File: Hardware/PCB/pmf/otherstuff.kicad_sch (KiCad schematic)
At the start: 66 parts, among them J10 Synth_power_2x5, J11 Conn_02x07_Odd_Even, J12 AudioJack2, J13 Conn_02x07_Odd_Even, J14 Conn_02x07_Odd_Even, J5 AudioJack2, J6 AudioJack2, J7 AudioJack2, J8 AudioJack2, J9 AudioJack2, SW1 SW_Rotary12, U2 TL072

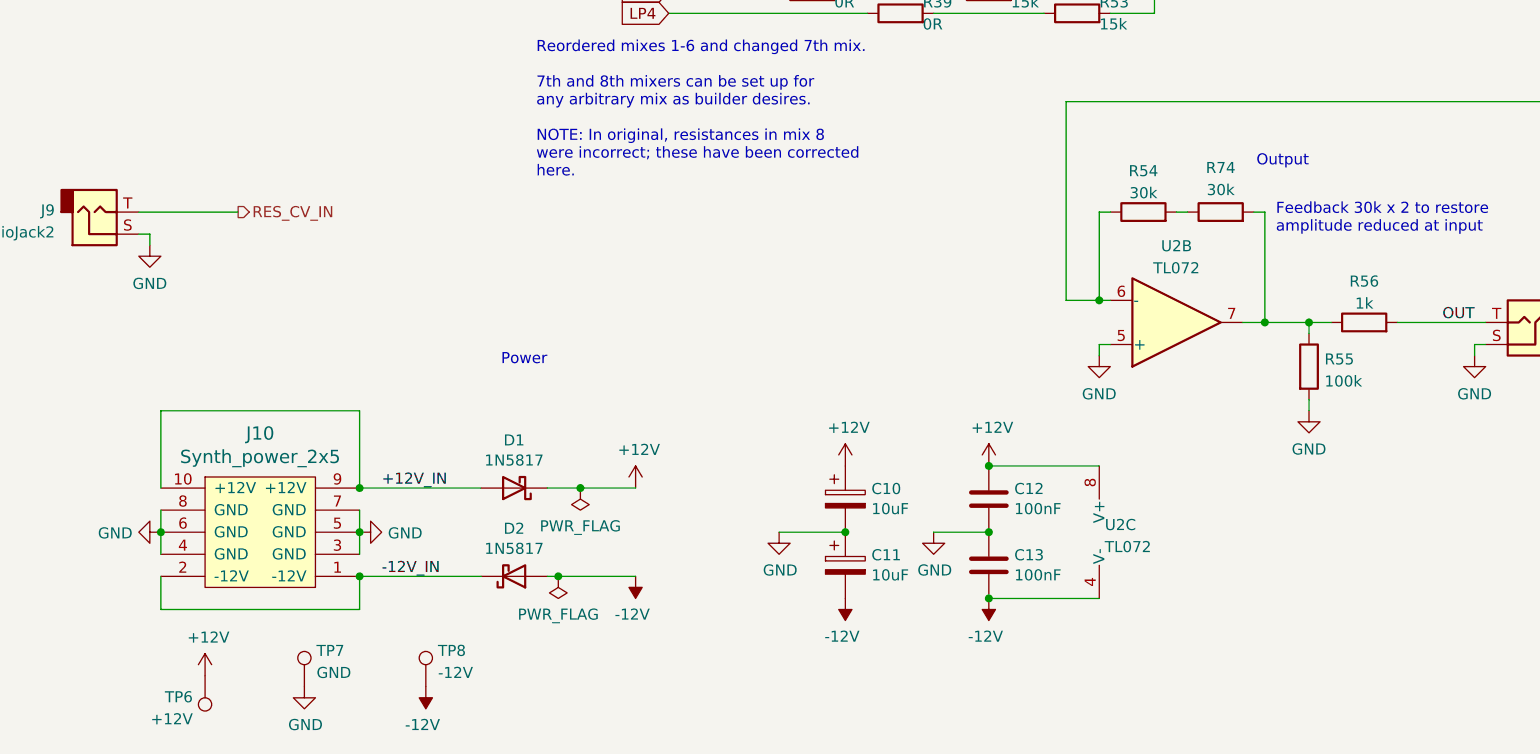
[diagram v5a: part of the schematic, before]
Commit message: CVf test point; disambiguate heirarchical symbols
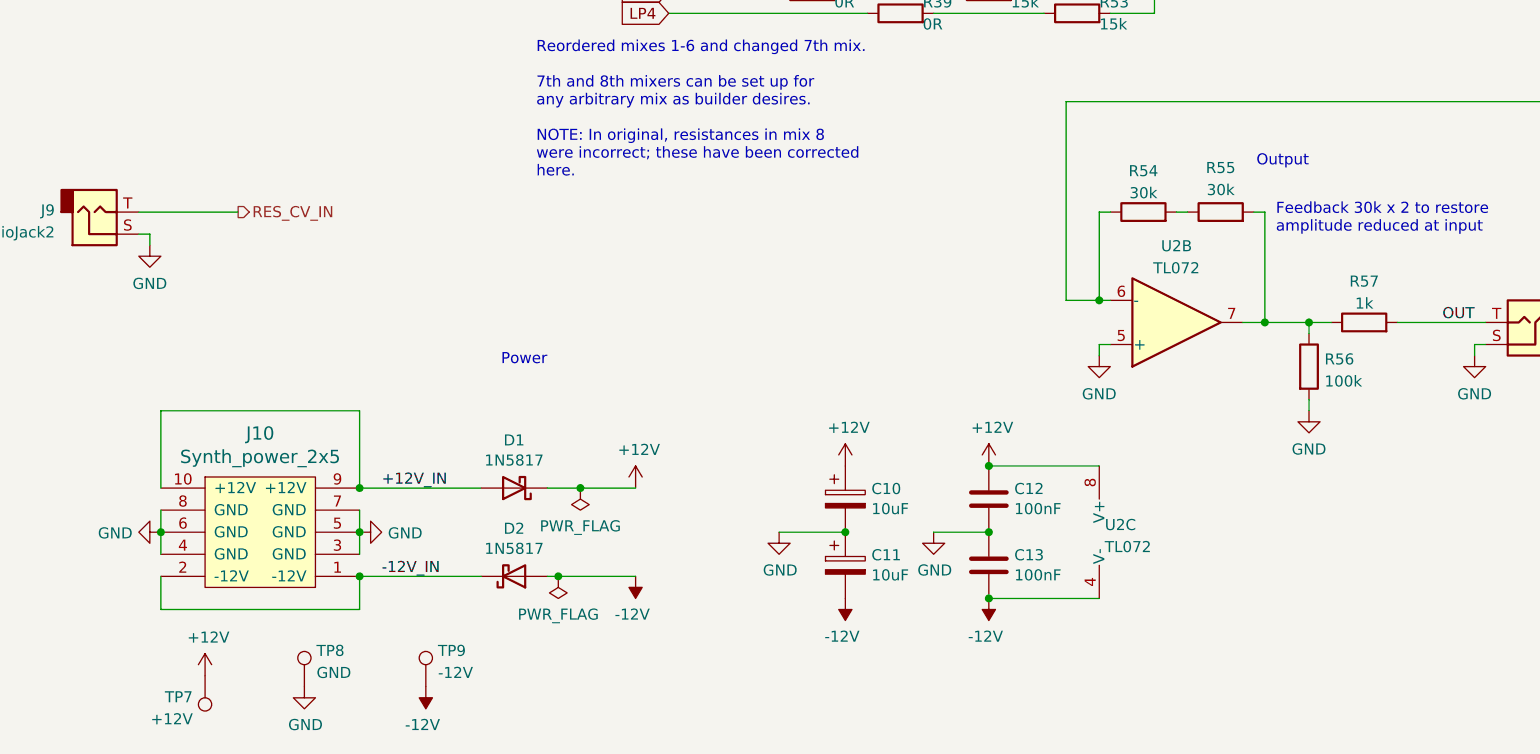
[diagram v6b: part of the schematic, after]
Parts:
- renumbered R74 to R55, R55 to R56, R56 to R57, TP6 to TP7, TP7 to TP8, TP8 to TP9
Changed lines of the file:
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@@
   (symbol (lib_id "AO_symbols:R") (at 172.72 160.02 0) (unit 1)
     (in_bom yes) (on_board yes) (dnp no) (fields_autoplaced)
-    (property "Reference" "R55" (at 174.498 159.1853 0)
+    (property "Reference" "R56" (at 174.498 159.1853 0)
       (effects (font (size 1.27 1.27)) (justify left))
     )
@@
       (project "pmf"
         (path "/1fce46f5-2003-4c7e-915f-b9b7dfc679d7/a180c6ca-d86a-4fef-be09-a6b0b94046eb"
-          (reference "R55") (unit 1)
+          (reference "R56") (unit 1)
         )
       )
@@
   (symbol (lib_id "AO_symbols:R") (at 179.07 154.94 90) (unit 1)
     (in_bom yes) (on_board yes) (dnp no) (fields_autoplaced)
-    (property "Reference" "R56" (at 179.07 150.2242 90)
+    (property "Reference" "R57" (at 179.07 150.2242 90)
       (effects (font (size 1.27 1.27)))
     )
@@
       (project "pmf"
         (path "/1fce46f5-2003-4c7e-915f-b9b7dfc679d7/a180c6ca-d86a-4fef-be09-a6b0b94046eb"
-          (reference "R56") (unit 1)
+          (reference "R57") (unit 1)
         )
       )
@@
   (symbol (lib_id "AO_symbols:TestPoint") (at 57.15 196.85 0) (unit 1)
     (in_bom no) (on_board yes) (dnp no) (fields_autoplaced)
-    (property "Reference" "TP7" (at 58.547 192.7133 0)
+    (property "Reference" "TP8" (at 58.547 192.7133 0)
       (effects (font (size 1.27 1.27)) (justify left))
     )
@@
       (project "pmf"
         (path "/1fce46f5-2003-4c7e-915f-b9b7dfc679d7/a180c6ca-d86a-4fef-be09-a6b0b94046eb"
-          (reference "TP7") (unit 1)
+          (reference "TP8") (unit 1)
         )
       )
@@
   (symbol (lib_id "AO_symbols:TestPoint") (at 71.12 196.85 0) (unit 1)
     (in_bom no) (on_board yes) (dnp no) (fields_autoplaced)
-    (property "Reference" "TP8" (at 72.517 192.7133 0)
+    (property "Reference" "TP9" (at 72.517 192.7133 0)
       (effects (font (size 1.27 1.27)) (justify left))
     )
@@
       (project "pmf"
         (path "/1fce46f5-2003-4c7e-915f-b9b7dfc679d7/a180c6ca-d86a-4fef-be09-a6b0b94046eb"
-          (reference "TP8") (unit 1)
+          (reference "TP9") (unit 1)
         )
       )
@@
   (symbol (lib_id "AO_symbols:R") (at 162.56 142.24 90) (unit 1)
     (in_bom yes) (on_board yes) (dnp no) (fields_autoplaced)
-    (property "Reference" "R74" (at 162.56 137.16 90)
+    (property "Reference" "R55" (at 162.56 137.16 90)
       (effects (font (size 1.27 1.27)))
     )
@@
       (project "pmf"
         (path "/1fce46f5-2003-4c7e-915f-b9b7dfc679d7/a180c6ca-d86a-4fef-be09-a6b0b94046eb"
-          (reference "R74") (unit 1)
+          (reference "R55") (unit 1)
         )
       )
@@
   (symbol (lib_id "AO_symbols:TestPoint") (at 45.72 195.58 0) (mirror x) (unit 1)
     (in_bom no) (on_board yes) (dnp no) (fields_autoplaced)
-    (property "Reference" "TP6" (at 44.323 198.0473 0)
+    (property "Reference" "TP7" (at 44.323 198.0473 0)
       (effects (font (size 1.27 1.27)) (justify right))
     )
@@
       (project "pmf"
         (path "/1fce46f5-2003-4c7e-915f-b9b7dfc679d7/a180c6ca-d86a-4fef-be09-a6b0b94046eb"
-          (reference "TP6") (unit 1)
-        )
-      )
+          (reference "TP7") (unit 1)
+        )
+      )

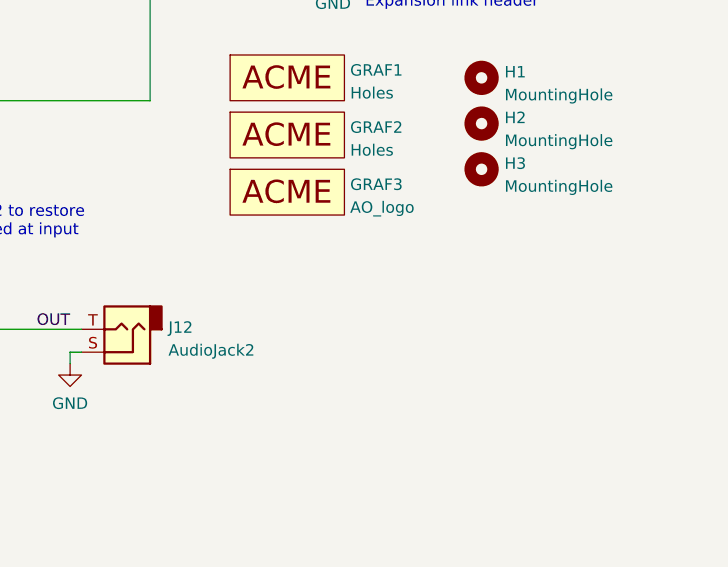
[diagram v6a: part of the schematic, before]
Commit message: Hardware symbols test
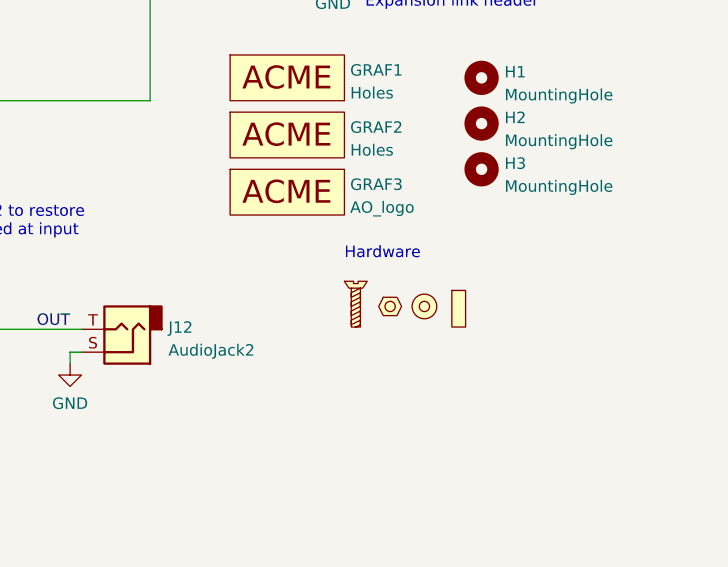
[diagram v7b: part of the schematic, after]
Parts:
- added M1: screw, symbol AO_symbols:Screw
- added M2: nut, symbol AO_symbols:Nut
- added M3: washer, symbol AO_symbols:Washer
- added M4: spacer, symbol AO_symbols:Spacer
- R28, R37, R43, R51: footprint pmf:R_Axial_DNF_L6.3mm_P10.16mm_Horizontal -> AO_tht:R_Axial_DIN0207_L6.3mm_D2.5mm_P10.16mm_Horizontal
- R30, R39, R42, R44, R50, R52: footprint pmf:Wire_Jumper_10.16 -> AO_tht:R_Axial_DIN0207_L6.3mm_D2.5mm_P10.16mm_Horizontal
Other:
- note added: "Hardware"
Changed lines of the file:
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@@
     (effects (font (size 1.27 1.27)) (justify right bottom))
+  )
+  (text "Hardware" (at 222.25 147.32 0)
+    (effects (font (size 1.27 1.27)) (justify left bottom))
   )
   (text "4 pole LP: {0, 0, 0, 0, 1}" (at 114.3 34.29 0)
@@
       (effects (font (size 1.27 1.27)) (justify right))
     )
-    (property "Footprint" "pmf:R_Axial_DNF_L6.3mm_P10.16mm_Horizontal" (at 146.05 104.648 90)
+    (property "Footprint" "AO_tht:R_Axial_DIN0207_L6.3mm_D2.5mm_P10.16mm_Horizontal" (at 146.05 104.648 90)
       (effects (font (size 1.27 1.27)) hide)
     )
@@
       (effects (font (size 1.27 1.27)) (justify right))
     )
-    (property "Footprint" "pmf:Wire_Jumper_10.16" (at 135.89 113.538 90)
+    (property "Footprint" "AO_tht:R_Axial_DIN0207_L6.3mm_D2.5mm_P10.16mm_Horizontal" (at 135.89 113.538 90)
       (effects (font (size 1.27 1.27)) hide)
     )
@@
       (effects (font (size 1.27 1.27)) (justify right))
     )
-    (property "Footprint" "pmf:Wire_Jumper_10.16" (at 135.89 97.028 90)
+    (property "Footprint" "AO_tht:R_Axial_DIN0207_L6.3mm_D2.5mm_P10.16mm_Horizontal" (at 135.89 97.028 90)
       (effects (font (size 1.27 1.27)) hide)
     )
@@
       (effects (font (size 1.27 1.27)) (justify right))
     )
-    (property "Footprint" "pmf:Wire_Jumper_10.16" (at 146.05 116.078 90)
+    (property "Footprint" "AO_tht:R_Axial_DIN0207_L6.3mm_D2.5mm_P10.16mm_Horizontal" (at 146.05 116.078 90)
       (effects (font (size 1.27 1.27)) hide)
     )
@@
     )
   )
+  (symbol (lib_id "AO_symbols:Washer") (at 231.14 152.4 0) (unit 1)
+    (in_bom yes) (on_board no) (dnp no) (fields_autoplaced)
+    (property "Reference" "M3" (at 231.394 148.082 0)
+      (effects (font (size 1.27 1.27)) hide)
+    )
+    (property "Value" "washer" (at 231.394 149.86 0)
+      (effects (font (size 1.27 1.27)) hide)
+    )
+    (property "Footprint" "" (at 231.14 152.4 0)
+      (effects (font (size 1.27 1.27)) hide)
+    )
+    (property "Datasheet" "" (at 231.14 152.4 0)
+      (effects (font (size 1.27 1.27)) hide)
+    )
+    (property "Description" "M3 washer" (at 231.14 152.4 0)
+      (effects (font (size 1.27 1.27)) hide)
+    )
+    (instances
+      (project "pmf"
+        (path "/1fce46f5-2003-4c7e-915f-b9b7dfc679d7/a180c6ca-d86a-4fef-be09-a6b0b94046eb"
+          (reference "M3") (unit 1)
+        )
+      )
+    )
+  )
   (symbol (lib_id "AO_symbols:R") (at 146.05 97.79 90) (unit 1)
     (in_bom yes) (on_board yes) (dnp no)
@@
       (effects (font (size 1.27 1.27)) (justify right))
     )
-    (property "Footprint" "pmf:Wire_Jumper_10.16" (at 146.05 99.568 90)
+    (property "Footprint" "AO_tht:R_Axial_DIN0207_L6.3mm_D2.5mm_P10.16mm_Horizontal" (at 146.05 99.568 90)
       (effects (font (size 1.27 1.27)) hide)
     )
@@
     )
   )
+  (symbol (lib_id "AO_symbols:Spacer") (at 234.95 152.4 0) (unit 1)
+    (in_bom yes) (on_board no) (dnp no) (fields_autoplaced)
+    (property "Reference" "M4" (at 234.95 148.082 0)
+      (effects (font (size 1.27 1.27)) hide)
+    )
+    (property "Value" "spacer" (at 234.95 149.606 0)
+      (effects (font (size 1.27 1.27)) hide)
+    )
+    (property "Footprint" "" (at 234.95 152.4 0)
+      (effects (font (size 1.27 1.27)) hide)
+    )
+    (property "Datasheet" "" (at 234.95 152.4 0)
+      (effects (font (size 1.27 1.27)) hide)
+    )
+    (property "Description" "M3 spacer FF 10 mm" (at 234.95 152.4 0)
+      (effects (font (size 1.27 1.27)) hide)
+    )
+    (instances
+      (project "pmf"
+        (path "/1fce46f5-2003-4c7e-915f-b9b7dfc679d7/a180c6ca-d86a-4fef-be09-a6b0b94046eb"
+          (reference "M4") (unit 1)
+        )
+      )
+    )
+  )
   (symbol (lib_id "AO_symbols:R") (at 115.57 100.33 90) (unit 1)
     (in_bom no) (on_board yes) (dnp yes)
@@
       (effects (font (size 1.27 1.27)) (justify right))
     )
-    (property "Footprint" "pmf:R_Axial_DNF_L6.3mm_P10.16mm_Horizontal" (at 115.57 102.108 90)
+    (property "Footprint" "AO_tht:R_Axial_DIN0207_L6.3mm_D2.5mm_P10.16mm_Horizontal" (at 115.57 102.108 90)
       (effects (font (size 1.27 1.27)) hide)
     )
@@
       (effects (font (size 1.27 1.27)) (justify right))
     )
-    (property "Footprint" "pmf:R_Axial_DNF_L6.3mm_P10.16mm_Horizontal" (at 125.73 104.648 90)
+    (property "Footprint" "AO_tht:R_Axial_DIN0207_L6.3mm_D2.5mm_P10.16mm_Horizontal" (at 125.73 104.648 90)
       (effects (font (size 1.27 1.27)) hide)
     )
@@
       (effects (font (size 1.27 1.27)) (justify right))
     )
-    (property "Footprint" "pmf:R_Axial_DNF_L6.3mm_P10.16mm_Horizontal" (at 135.89 102.108 90)
+    (property "Footprint" "AO_tht:R_Axial_DIN0207_L6.3mm_D2.5mm_P10.16mm_Horizontal" (at 135.89 102.108 90)
       (effects (font (size 1.27 1.27)) hide)
     )
@@
       (effects (font (size 1.27 1.27)) (justify right))
     )
-    (property "Footprint" "pmf:Wire_Jumper_10.16" (at 115.57 118.618 90)
+    (property "Footprint" "AO_tht:R_Axial_DIN0207_L6.3mm_D2.5mm_P10.16mm_Horizontal" (at 115.57 118.618 90)
       (effects (font (size 1.27 1.27)) hide)
     )
@@
         (path "/1fce46f5-2003-4c7e-915f-b9b7dfc679d7/a180c6ca-d86a-4fef-be09-a6b0b94046eb"
           (reference "TP9") (unit 1)
+        )
+      )
+    )
+  )
+  (symbol (lib_id "AO_symbols:Nut") (at 227.33 152.4 0) (unit 1)
+    (in_bom yes) (on_board no) (dnp no) (fields_autoplaced)
+    (property "Reference" "M2" (at 227.33 148.336 0)
+      (effects (font (size 1.27 1.27)) hide)
+    )
+    (property "Value" "nut" (at 227.33 150.114 0)
+      (effects (font (size 1.27 1.27)) hide)
+    )
+    (property "Footprint" "" (at 227.33 152.4 0)
+      (effects (font (size 1.27 1.27)) hide)
+    )
+    (property "Datasheet" "" (at 227.33 152.4 0)
+      (effects (font (size 1.27 1.27)) hide)
+    )
+    (property "Description" "M3 nut" (at 227.33 152.4 0)
+      (effects (font (size 1.27 1.27)) hide)
+    )
+    (instances
+      (project "pmf"
+        (path "/1fce46f5-2003-4c7e-915f-b9b7dfc679d7/a180c6ca-d86a-4fef-be09-a6b0b94046eb"
+          (reference "M2") (unit 1)
         )
       )
@@
     )
   )
+  (symbol (lib_id "AO_symbols:Screw") (at 223.52 152.4 0) (unit 1)
+    (in_bom yes) (on_board no) (dnp no) (fields_autoplaced)
+    (property "Reference" "M1" (at 223.52 147.32 0)
+      (effects (font (size 1.27 1.27)) hide)
+    )
+    (property "Value" "screw" (at 223.774 148.59 0)
+      (effects (font (size 1.27 1.27)) hide)
+    )
+    (property "Footprint" "" (at 223.52 152.4 0)
+      (effects (font (size 1.27 1.27)) hide)
+    )
+    (property "Datasheet" "" (at 223.52 152.4 0)
+      (effects (font (size 1.27 1.27)) hide)
+    )
+    (property "Description" "M3 machine screw 6 mm" (at 223.52 152.4 0)
+      (effects (font (size 1.27 1.27)) hide)
+    )
+    (instances
+      (project "pmf"
+        (path "/1fce46f5-2003-4c7e-915f-b9b7dfc679d7/a180c6ca-d86a-4fef-be09-a6b0b94046eb"
+          (reference "M1") (unit 1)
+        )
+      )
+    )
+  )
   (symbol (lib_id "AO_symbols:MountingHole") (at 237.49 137.16 0) (unit 1)
     (in_bom no) (on_board yes) (dnp no) (fields_autoplaced)
@@
       (effects (font (size 1.27 1.27)) (justify right))
     )
-    (property "Footprint" "pmf:Wire_Jumper_10.16" (at 125.73 121.158 90)
-      (effects (font (size 1.27 1.27)) hide)
-    )
+    (property "Footprint" "AO_tht:R_Axial_DIN0207_L6.3mm_D2.5mm_P10.16mm_Horizontal" (at 125.73 121.158 90)
+      (effects (font (size 1.27 1.27)) hide)
+    )

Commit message: Return to smaller trimmer values; make core schematic clearer; restore munged footprints
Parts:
- R28, R37, R43, R51: footprint AO_tht:R_Axial_DIN0207_L6.3mm_D2.5mm_P10.16mm_Horizontal -> pmf:R_Axial_DNF_L6.3mm_P10.16mm_Horizontal
- R30, R39, R42, R44, R50, R52: footprint AO_tht:R_Axial_DIN0207_L6.3mm_D2.5mm_P10.16mm_Horizontal -> pmf:Wire_Jumper_10.16
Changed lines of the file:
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@@
       (effects (font (size 1.27 1.27)) (justify right))
     )
-    (property "Footprint" "AO_tht:R_Axial_DIN0207_L6.3mm_D2.5mm_P10.16mm_Horizontal" (at 146.05 104.648 90)
+    (property "Footprint" "pmf:R_Axial_DNF_L6.3mm_P10.16mm_Horizontal" (at 146.05 104.648 90)
       (effects (font (size 1.27 1.27)) hide)
     )
@@
       (effects (font (size 1.27 1.27)) (justify right))
     )
-    (property "Footprint" "AO_tht:R_Axial_DIN0207_L6.3mm_D2.5mm_P10.16mm_Horizontal" (at 135.89 113.538 90)
+    (property "Footprint" "pmf:Wire_Jumper_10.16" (at 135.89 113.538 90)
       (effects (font (size 1.27 1.27)) hide)
     )
@@
       (effects (font (size 1.27 1.27)) (justify right))
     )
-    (property "Footprint" "AO_tht:R_Axial_DIN0207_L6.3mm_D2.5mm_P10.16mm_Horizontal" (at 135.89 97.028 90)
+    (property "Footprint" "pmf:Wire_Jumper_10.16" (at 135.89 97.028 90)
       (effects (font (size 1.27 1.27)) hide)
     )
@@
       (effects (font (size 1.27 1.27)) (justify right))
     )
-    (property "Footprint" "AO_tht:R_Axial_DIN0207_L6.3mm_D2.5mm_P10.16mm_Horizontal" (at 146.05 116.078 90)
+    (property "Footprint" "pmf:Wire_Jumper_10.16" (at 146.05 116.078 90)
       (effects (font (size 1.27 1.27)) hide)
     )
@@
       (effects (font (size 1.27 1.27)) (justify right))
     )
-    (property "Footprint" "AO_tht:R_Axial_DIN0207_L6.3mm_D2.5mm_P10.16mm_Horizontal" (at 146.05 99.568 90)
+    (property "Footprint" "pmf:Wire_Jumper_10.16" (at 146.05 99.568 90)
       (effects (font (size 1.27 1.27)) hide)
     )
@@
       (effects (font (size 1.27 1.27)) (justify right))
     )
-    (property "Footprint" "AO_tht:R_Axial_DIN0207_L6.3mm_D2.5mm_P10.16mm_Horizontal" (at 115.57 102.108 90)
+    (property "Footprint" "pmf:R_Axial_DNF_L6.3mm_P10.16mm_Horizontal" (at 115.57 102.108 90)
       (effects (font (size 1.27 1.27)) hide)
     )
@@
       (effects (font (size 1.27 1.27)) (justify right))
     )
-    (property "Footprint" "AO_tht:R_Axial_DIN0207_L6.3mm_D2.5mm_P10.16mm_Horizontal" (at 125.73 104.648 90)
+    (property "Footprint" "pmf:R_Axial_DNF_L6.3mm_P10.16mm_Horizontal" (at 125.73 104.648 90)
       (effects (font (size 1.27 1.27)) hide)
     )
@@
       (effects (font (size 1.27 1.27)) (justify right))
     )
-    (property "Footprint" "AO_tht:R_Axial_DIN0207_L6.3mm_D2.5mm_P10.16mm_Horizontal" (at 135.89 102.108 90)
+    (property "Footprint" "pmf:R_Axial_DNF_L6.3mm_P10.16mm_Horizontal" (at 135.89 102.108 90)
       (effects (font (size 1.27 1.27)) hide)
     )
@@
       (effects (font (size 1.27 1.27)) (justify right))
     )
-    (property "Footprint" "AO_tht:R_Axial_DIN0207_L6.3mm_D2.5mm_P10.16mm_Horizontal" (at 115.57 118.618 90)
+    (property "Footprint" "pmf:Wire_Jumper_10.16" (at 115.57 118.618 90)
       (effects (font (size 1.27 1.27)) hide)
     )
@@
       (effects (font (size 1.27 1.27)) (justify right))
     )
-    (property "Footprint" "AO_tht:R_Axial_DIN0207_L6.3mm_D2.5mm_P10.16mm_Horizontal" (at 125.73 121.158 90)
-      (effects (font (size 1.27 1.27)) hide)
-    )
+    (property "Footprint" "pmf:Wire_Jumper_10.16" (at 125.73 121.158 90)
+      (effects (font (size 1.27 1.27)) hide)
+    )
